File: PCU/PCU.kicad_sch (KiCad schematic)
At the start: 1 part, among them J4 MR30PW-M

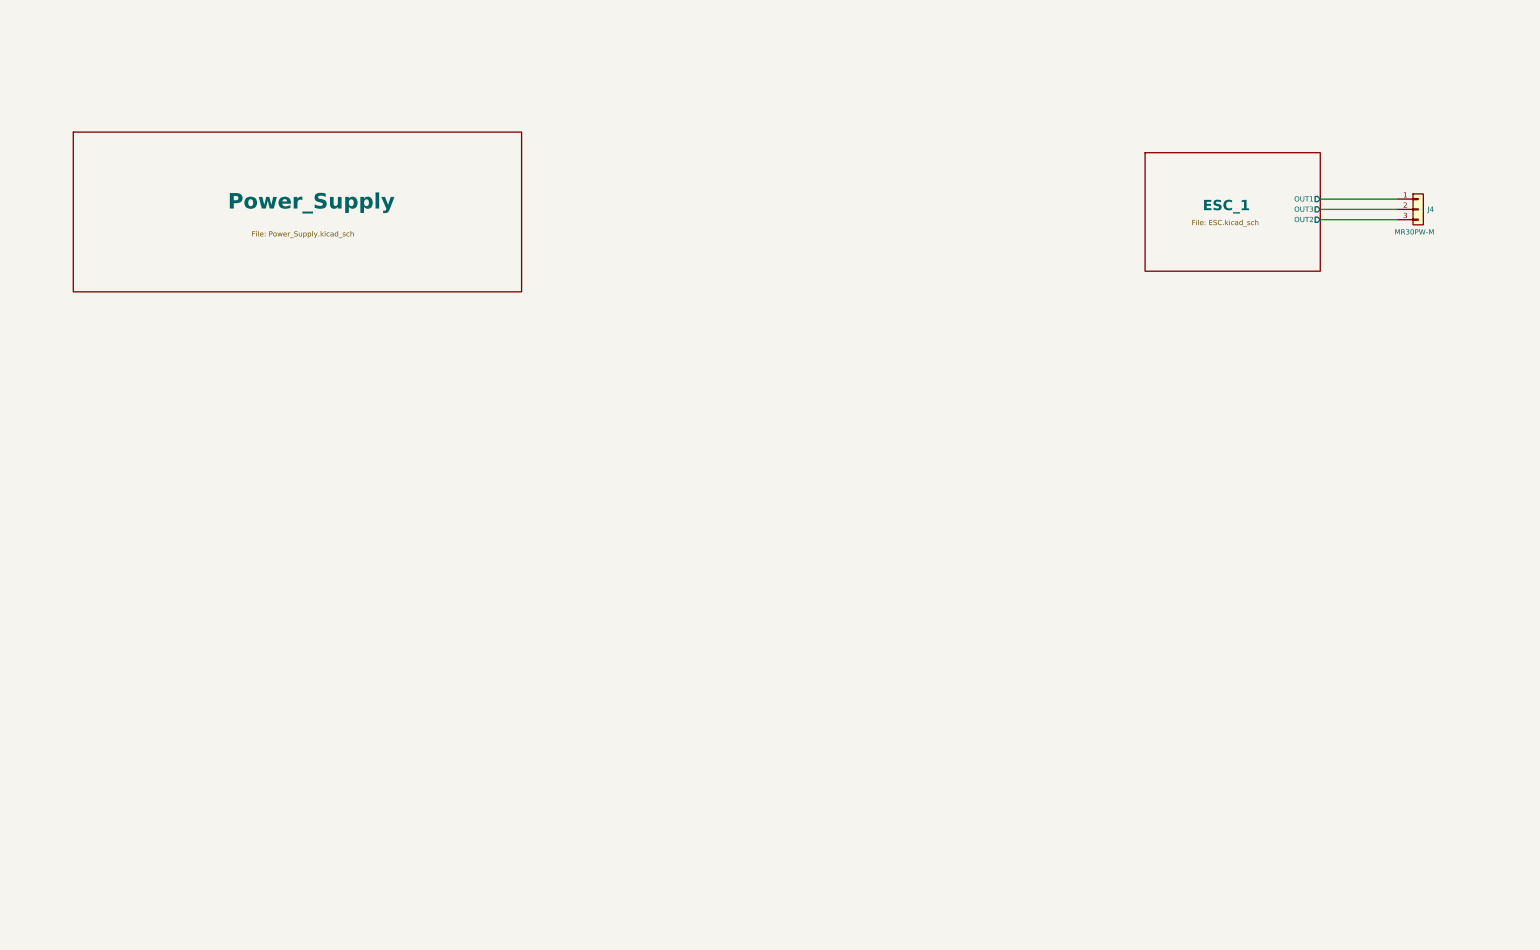
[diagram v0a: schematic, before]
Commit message: ESC Block Updated
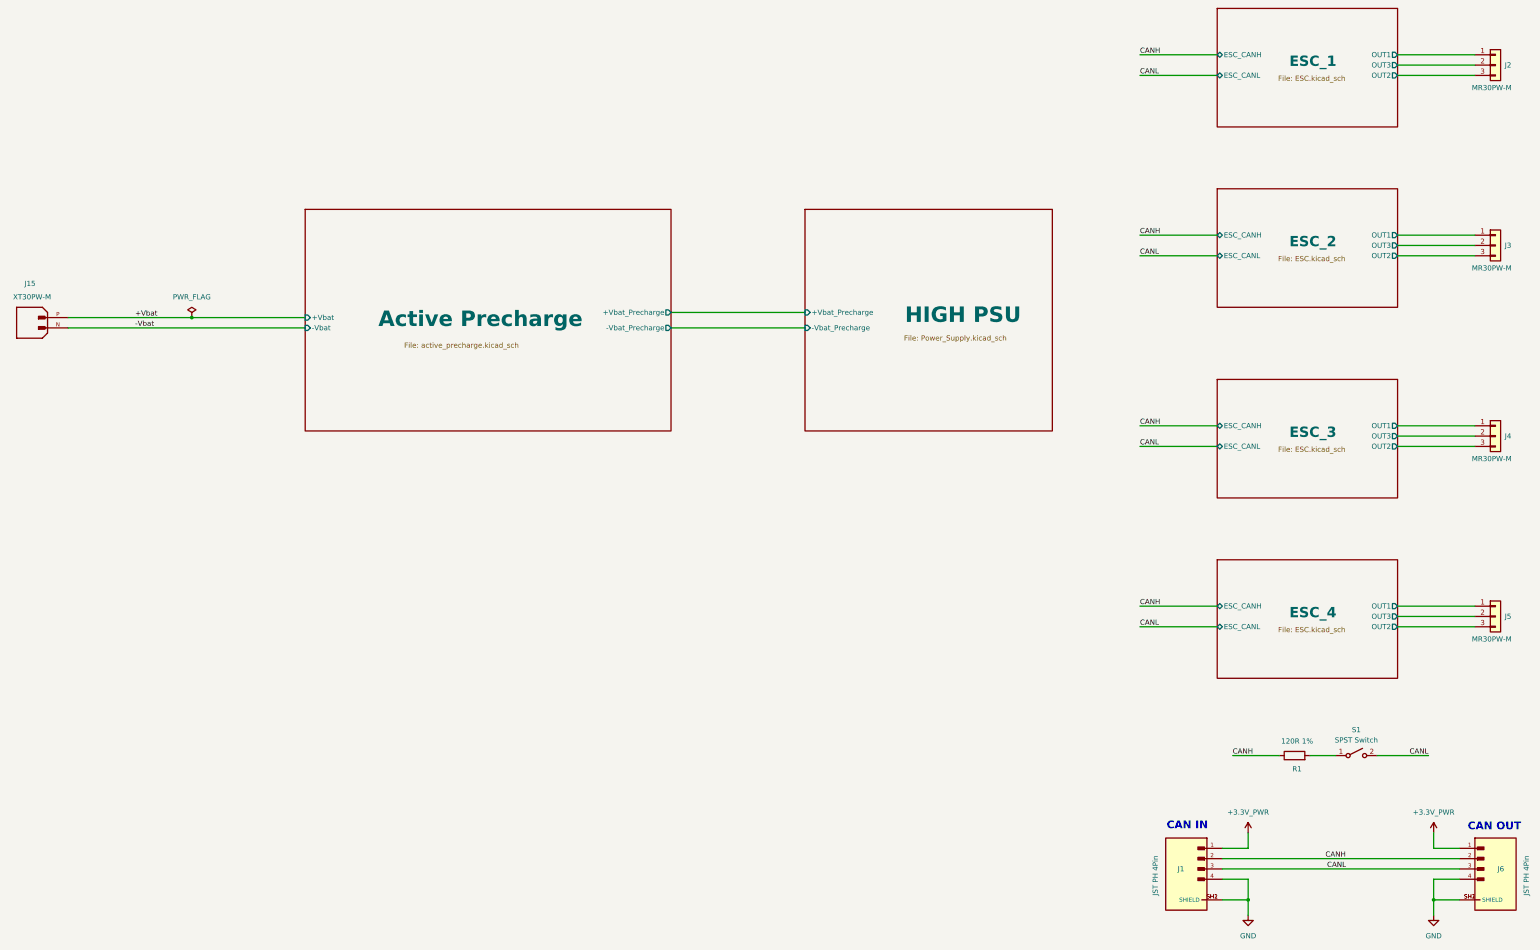
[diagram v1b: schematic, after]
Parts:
- added J1, J6: JST PH 4Pin, BassinaLib_Connectors:S4B-PH-SM4-TB, symbol BassinaLib_Connectors:S4B-PH-SM4-TB_LF__SN_
- added J15: XT30PW-M, BassinaLib_Connectors:AMASS_XT30PW-M, symbol BassinaLib_Connectors:XT30PW-M
- added J3, J4, J5: MR30PW-M, Connector_AMASS:AMASS_MR30PW-M_1x03_P3.50mm_Horizontal, symbol Connector_Generic:Conn_01x03
- added R1: 120R 1%, Resistor_SMD:R_0603_1608Metric, symbol Device:R
- added S1: SPST Switch, BassinaLib_Switch:DS04254201BKSMT, symbol BassinaLib_Switch:DS04-254-2-01BK-SMT
- renumbered J4 to J2
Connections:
- new net: R1.2, S1.1
- new net +3.3V_PWR: J1.1, J6.1
- new net +Vbat: J15.P
- new net -Vbat: J15.N
- new net CANH: J1.2, J6.2, R1.1
- new net CANL: J1.3, J6.3, S1.2
- new net ESC_2/OUT1: J3.1 (Pin_1)
- new net ESC_2/OUT2: J3.3 (Pin_3)
- new net ESC_2/OUT3: J3.2 (Pin_2)
- new net ESC_3/OUT1: J4.1 (Pin_1)
- new net ESC_3/OUT2: J4.3 (Pin_3)
- new net ESC_3/OUT3: J4.2 (Pin_2)
- new net ESC_4/OUT1: J5.1 (Pin_1)
- new net ESC_4/OUT2: J5.3 (Pin_3)
- new net ESC_4/OUT3: J5.2 (Pin_2)
- new net GND: J1.4, J1.SH1 (SHIELD), J1.SH2 (SHIELD), J6.4, J6.SH1 (SHIELD), J6.SH2 (SHIELD)
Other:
- sheet Power_Supply renamed HIGH PSU
- added sheet Active Precharge (active_precharge.kicad_sch)
- added sheet ESC_2 (ESC.kicad_sch)
- added sheet ESC_3 (ESC.kicad_sch)
- added sheet ESC_4 (ESC.kicad_sch)
- sheet ESC_1 ports: added ESC_CANH, ESC_CANL; removed none
- sheet HIGH PSU ports: added +Vbat_Precharge, -Vbat_Precharge; removed none
- note added: "CAN IN"
- note added: "CAN OUT"
- moved on the sheet: J2

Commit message: high power supply block
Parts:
- renumbered J15 to J1, J1 to J2, J2 to J3, J3 to J4, J4 to J5, J5 to J6, J6 to J7
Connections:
- net +3.3V_PWR renamed +3.3V_Digital
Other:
- added sheet Logic PSU (logic_power_supply.kicad_sch)
- added sheet Supervisor (Supervisor.kicad_sch)
- sheet HIGH PSU: file Power_Supply.kicad_sch -> high_power_supply.kicad_sch
- moved on the sheet: J1

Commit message: Logic PSU Completed
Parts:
- removed J1: XT30PW-M, BassinaLib_Connectors:AMASS_XT30PW-M, symbol BassinaLib_Connectors:XT30PW-M
- removed J2, J7: JST PH 4Pin, BassinaLib_Connectors:S4B-PH-SM4-TB, symbol BassinaLib_Connectors:S4B-PH-SM4-TB_LF__SN_
- added D51: TVS 33V, 600W, BassingaLib_TVS:DIONM5436X244N, symbol BassingaLib_TVS:SMBJ33CA
- added J1: XT60PW-M, BassinaLib_Connectors:AMASS_XT60PW-M, symbol BassinaLib_Connectors:XT60PW-M
- added J19, J2: B4B-PH-K-S_LF__SN_, BassinaLib_Connectors:JST_B4B-PH-K-S_LF__SN_, symbol BassinaLib_Connectors:B4B-PH-K-S_LF__SN_
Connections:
- net +Vbat: now also D51.2, J1.P (+)
- net -Vbat: now also D51.1, J1.N (-)
- net CANH: now also J19.2, J2.2
- net CANL: now also J19.3, J2.3
- net GND: now also J19.4, J2.4
- new net +3.3V_Logic: J19.1, J2.1
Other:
- sheet Active Precharge ports: added EN_Precharge, EN_mainBus, mainBus_nFault; removed none
- sheet HIGH PSU ports: added V12_Mesure, V3.3_Mesure, Vbus_Mesure; removed none
- sheet Logic PSU ports: added V12Logic_Mesure, V3.3Logic_Mesure, V5Logic_Mesure, Vbat_Mesure; removed none
- sheet Supervisor ports: added EN_Precharge, EN_mainBus, V12Logic_Mesure, V12_Mesure, V3.3Logic_Mesure, V3.3_Mesure, V5Logic_Mesure, Vbat_Mesure, Vbus_Mesure, mainBus_nFault; removed none

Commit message: Supervisor Block
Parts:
- removed J19: B4B-PH-K-S_LF__SN_, BassinaLib_Connectors:JST_B4B-PH-K-S_LF__SN_, symbol BassinaLib_Connectors:B4B-PH-K-S_LF__SN_
- removed J3, J4, J5, J6: MR30PW-M, Connector_AMASS:AMASS_MR30PW-M_1x03_P3.50mm_Horizontal, symbol Connector_Generic:Conn_01x03
- added D2, D3: PESD2CANFD24V-TR, BassingaLib_TVS:SOT95P230X110-3N, symbol BassingaLib_TVS:PESD2CANFD24V-TR
- added J2: B4B-PH-K-S_LF__SN_, BassinaLib_Connectors:JST_B4B-PH-K-S_LF__SN_, symbol BassinaLib_Connectors:B4B-PH-K-S_LF__SN_
- added J4, J5, J6, J7: MR30PW-FB, BassinaLib_Connectors:MR30PWFB, symbol BassinaLib_Connectors:MR30PW-FB
- renumbered D51 to D1, J2 to J3
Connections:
- net -Vbat is gone; now on net GND: D1.1, J1.N (-)
- net +3.3V_Logic: now also J2.1
- net CANH: now also D2.1, D3.1, J2.2
- net CANL: now also D2.2, D3.2, J2.3
- net ESC_1/OUT1: now also J4.1
- net ESC_1/OUT2: now also J4.3
- net ESC_1/OUT3: now also J4.2
- net ESC_2/OUT1: now also J5.1
- net ESC_2/OUT2: now also J5.3
- net ESC_2/OUT3: now also J5.2
- net ESC_3/OUT1: now also J6.1
- net ESC_3/OUT2: now also J6.3
- net ESC_3/OUT3: now also J6.2
- net ESC_4/OUT1: now also J7.1
- net ESC_4/OUT2: now also J7.3
- net ESC_4/OUT3: now also J7.2
- net GND: now also D2.3, D3.3, J2.4
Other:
- sheet Active Precharge ports: added +Vbus; removed +Vbat_Precharge, -Vbat, -Vbat_Precharge
- sheet HIGH PSU ports: added +Vbus; removed +Vbat_Precharge, -Vbat_Precharge
- sheet Logic PSU ports: added none; removed -Vbat
- sheet Supervisor ports: added SPV_CANH, SPV_CANL; removed none
- note added: "FD-CAN Network"
- moved on the sheet: D1, J1, J3, R1, S1
